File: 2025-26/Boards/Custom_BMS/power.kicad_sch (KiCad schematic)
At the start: 23 parts, among them J2 Conn_01x02_Pin, Q2 AO3401A, U2 TPS563300, U4 AMS1117-3.3

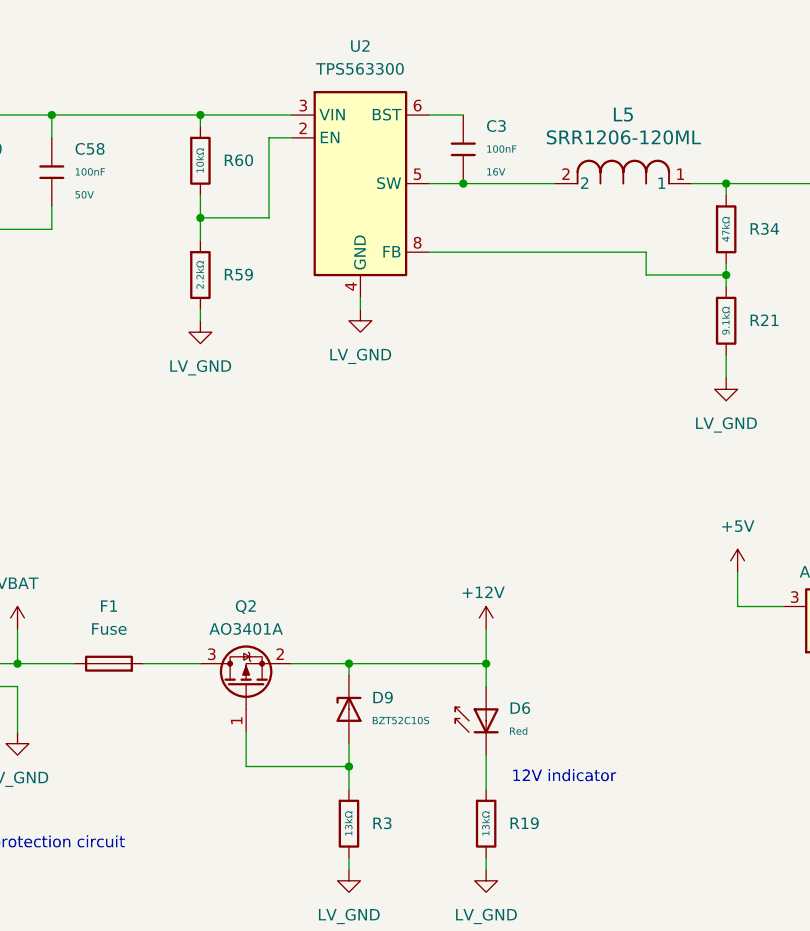
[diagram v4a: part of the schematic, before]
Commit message: more layout progress, stm32, power, etc.
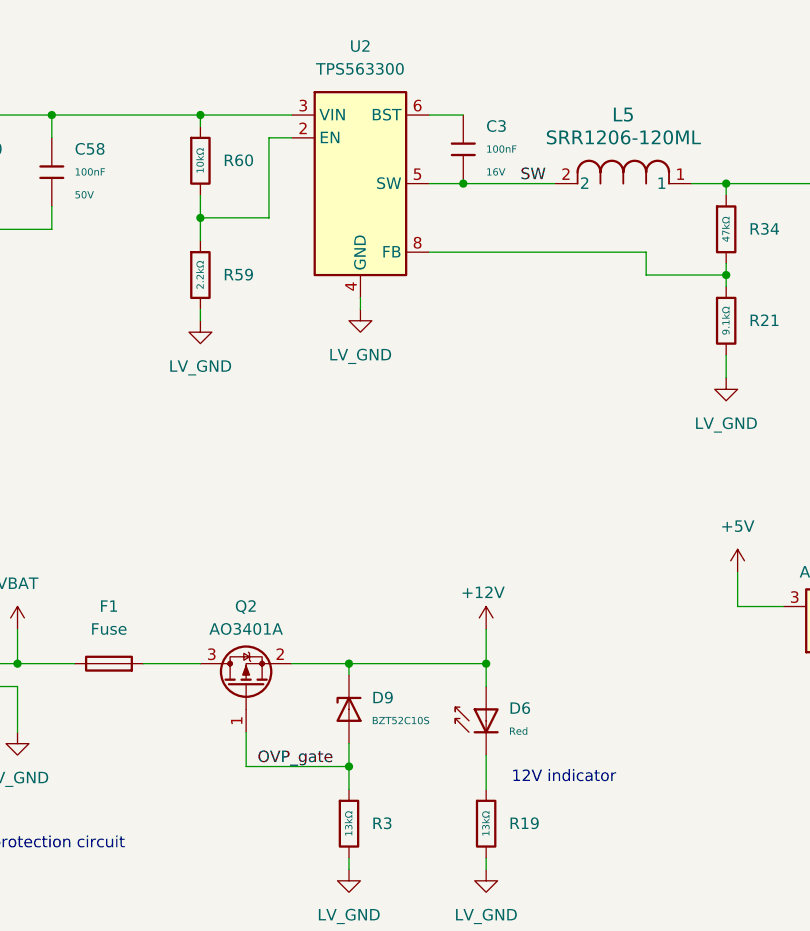
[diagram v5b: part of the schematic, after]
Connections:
- net SW: now reaches C3.2, L5.2, U2.5 (SW)
- net OVP_gate: now reaches D9.2, Q2.1 (G), R3.1
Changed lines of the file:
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@@
+		)
+	)
+	(label "SW"
+		(at 114.3 80.01 0)
+		(effects
+			(font
+				(size 1.27 1.27)
+			)
+			(justify left bottom)
+		)
+	)
+	(label "OVP_gate"
+		(at 85.09 144.78 0)
+		(effects
+			(font
+				(size 1.27 1.27)
+			)
+			(justify left bottom)
 		)
 	)

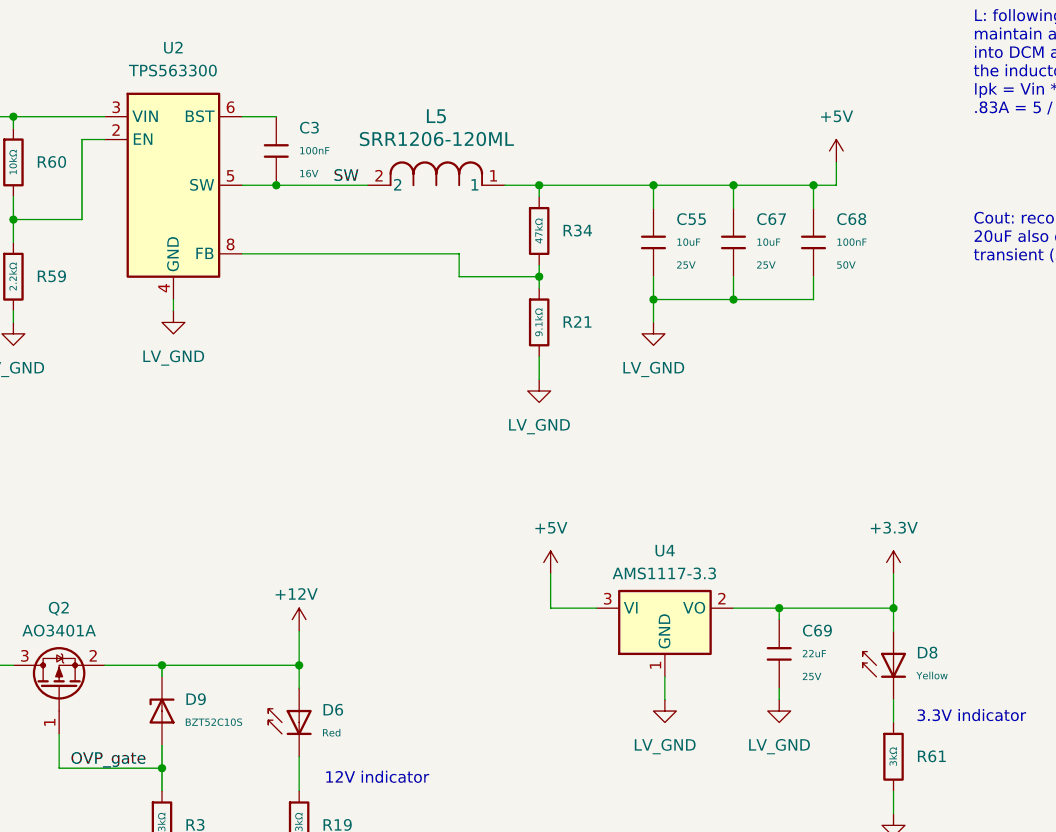
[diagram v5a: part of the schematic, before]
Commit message: finishe difrst draft layout
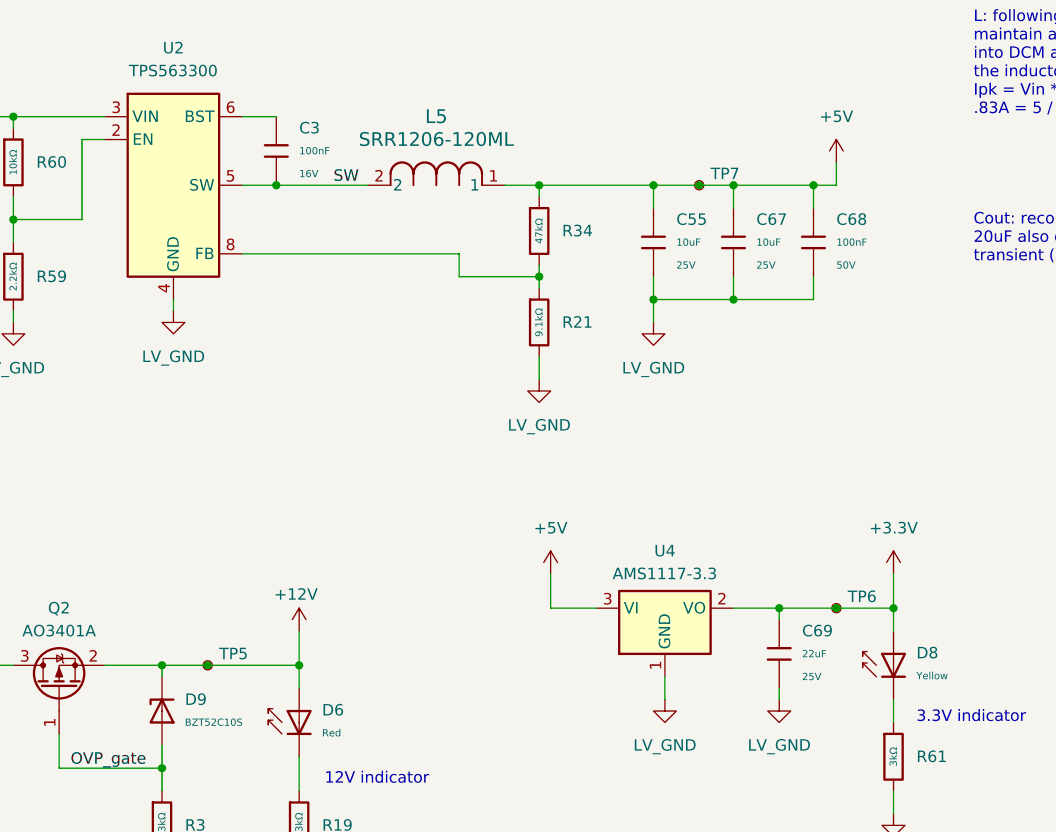
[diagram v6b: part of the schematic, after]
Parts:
- added TP5, TP6, TP7: TestPoint_Small, TestPoint:TestPoint_Pad_D1.0mm, symbol Connector:TestPoint_Small
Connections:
- net +12V: now also TP5.1
- net +3.3V: now also TP6.1
- net +5V: now also TP7.1

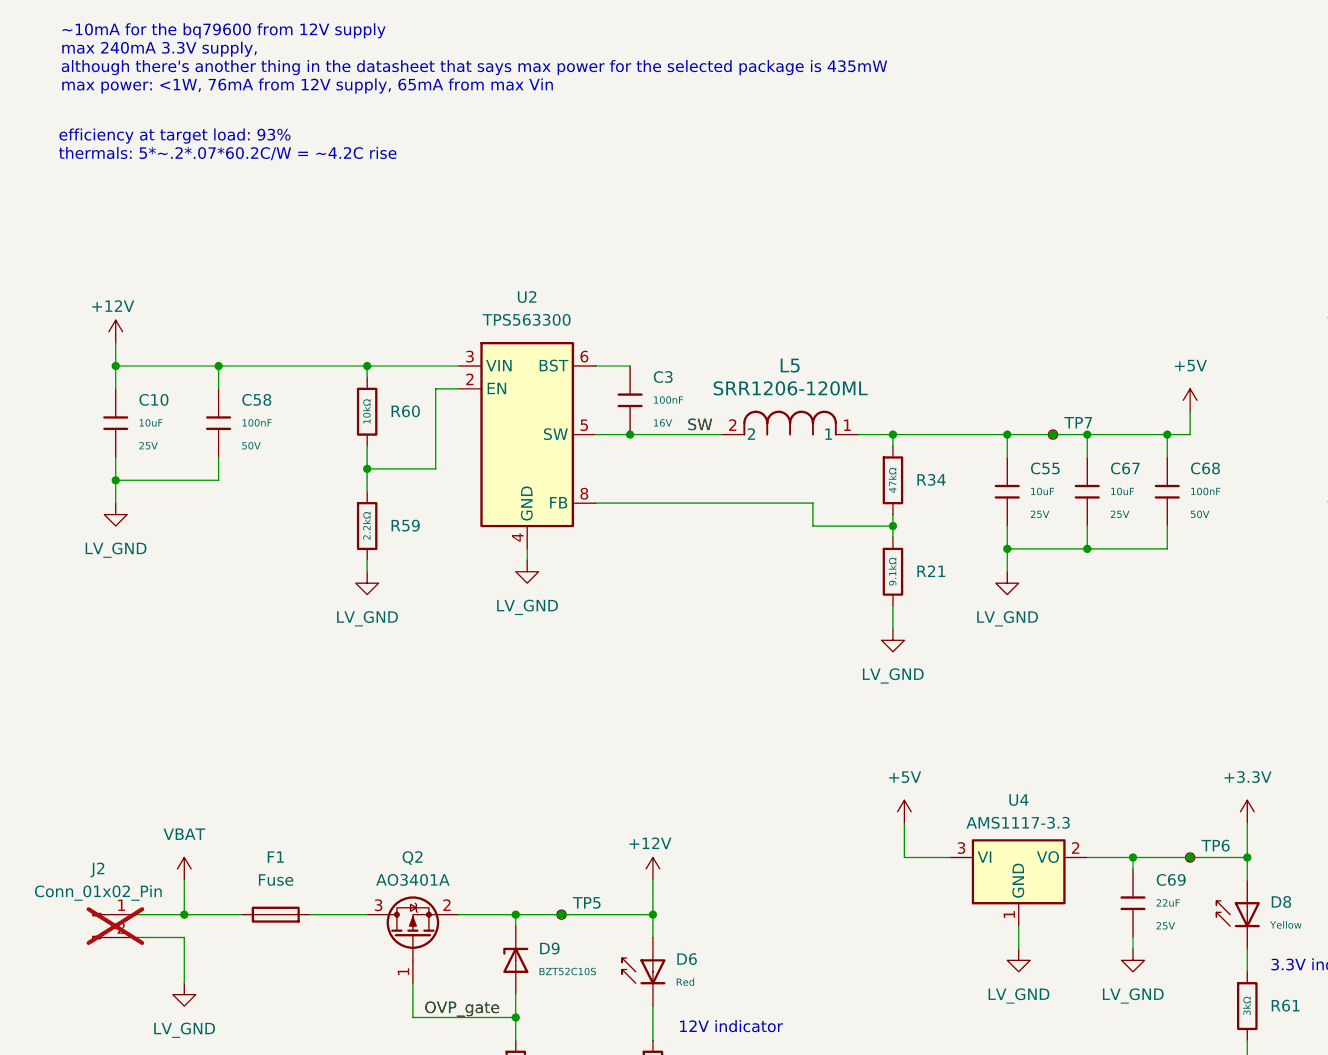
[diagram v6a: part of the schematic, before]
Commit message: fixed some layout and schematic issues
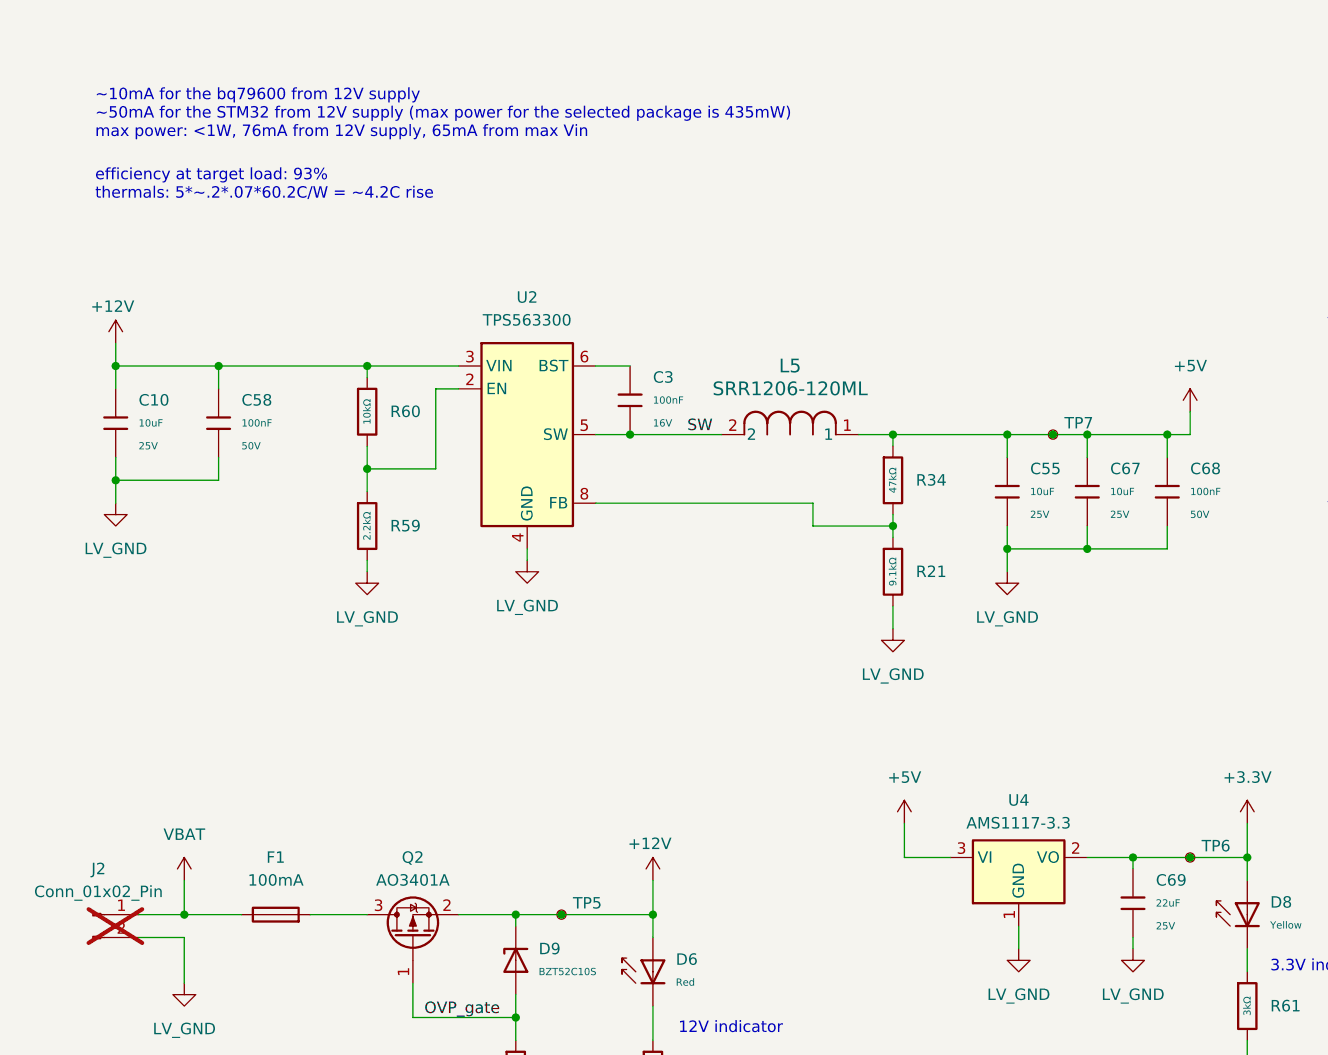
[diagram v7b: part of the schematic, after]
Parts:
- F1: value Fuse -> 100mA
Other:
- note added: "~10mA for the bq79600 from 12V supply ~50mA for the STM32 from 12V supply (max power for the selected package is 435mW) max power: <1W, 76mA from 12V supply, 65mA from max Vin"
- note removed: "~10mA for the bq79600 from 12V supply max 240mA 3.3V supply, although there's another thing in the datasheet that says max power for the selected package is 435mW max power: <1W, 76mA from 12V supply, 65mA from max Vin"
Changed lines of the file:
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@@
 	(text "efficiency at target load: 93%\nthermals: 5*~.2*.07*60.2C/W = ~4.2C rise"
 		(exclude_from_sim no)
-		(at 44.45 48.006 0)
+		(at 48.514 52.324 0)
 		(effects
 			(font
@@
 		)
 	)
-	(text "~10mA for the bq79600 from 12V supply\nmax 240mA 3.3V supply, \nalthough there's another thing in the datasheet that says max power for the selected package is 435mW\nmax power: <1W, 76mA from 12V supply, 65mA from max Vin\n"
+	(text "~10mA for the bq79600 from 12V supply\n~50mA for the STM32 from 12V supply (max power for the selected package is 435mW)\nmax power: <1W, 76mA from 12V supply, 65mA from max Vin\n"
 		(exclude_from_sim no)
-		(at 44.704 38.354 0)
+		(at 48.514 44.45 0)
 		(effects
 			(font
@@
 			)
 		)
-		(property "Value" "Fuse"
+		(property "Value" "100mA"
 			(at 68.58 129.54 90)
 			(effects
